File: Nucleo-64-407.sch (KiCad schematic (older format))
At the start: 70 parts, among them J1 SWD, J3 USB_B_Micro, J4 Serial 0, J5 EXP1, J6 EXP2, J7 EXP3, J8 EXP4, SW1 RESET, SW2 BOOT, U1 STM32F407VETx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

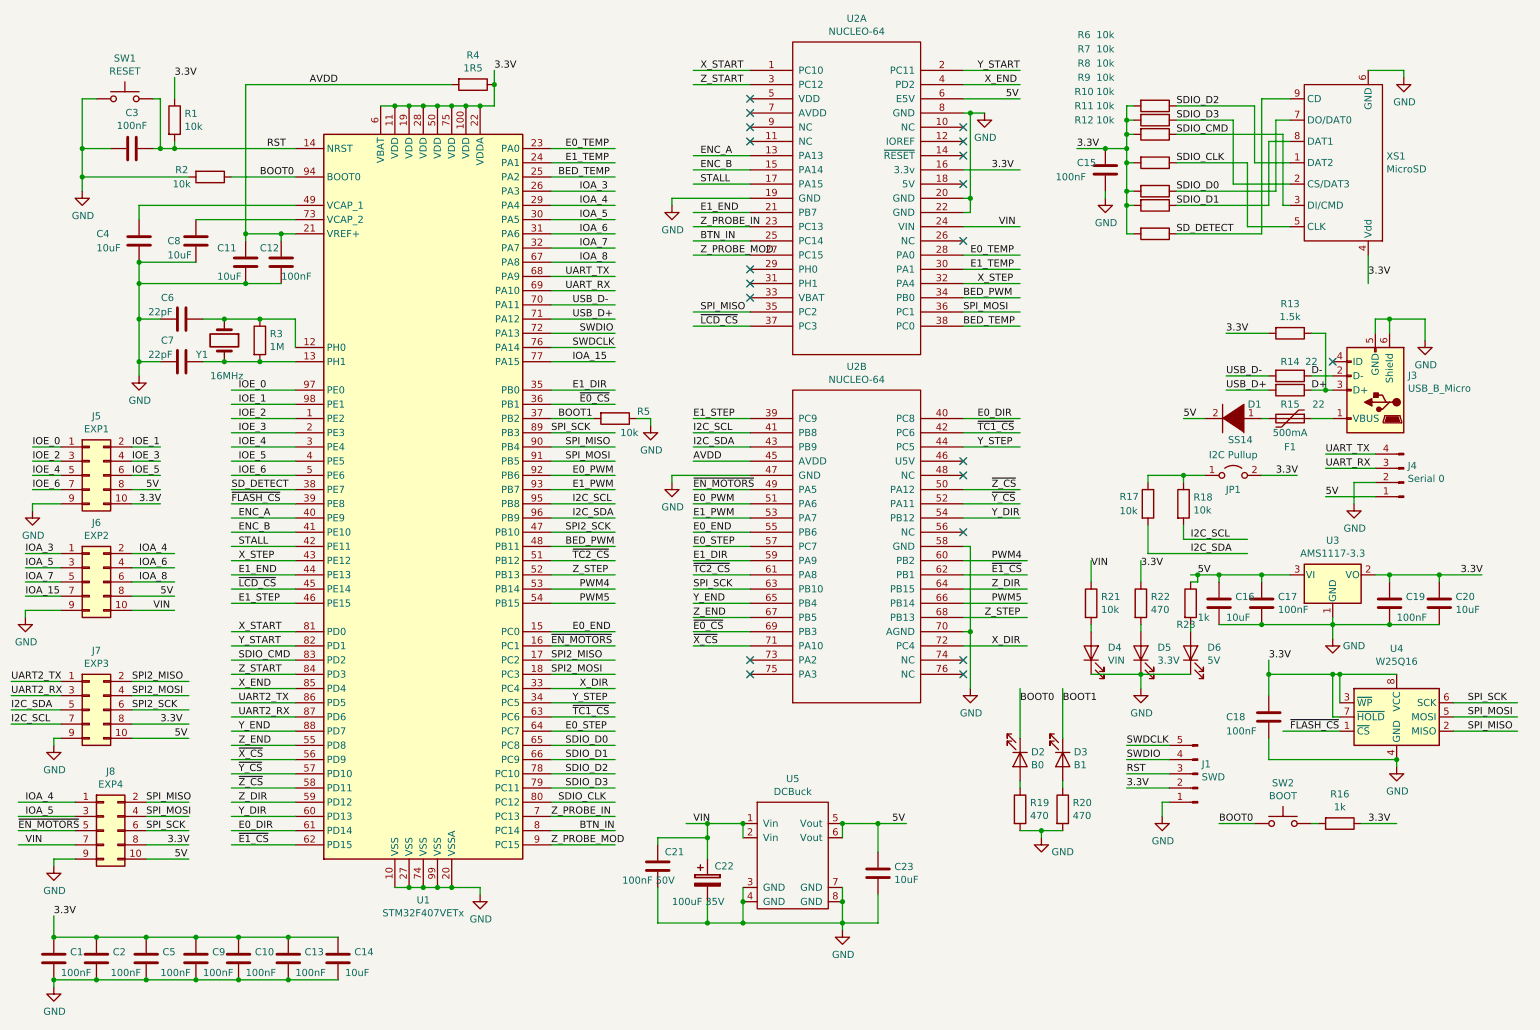
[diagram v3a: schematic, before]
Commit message: Improve the NUCLEO-64 layout a bit.
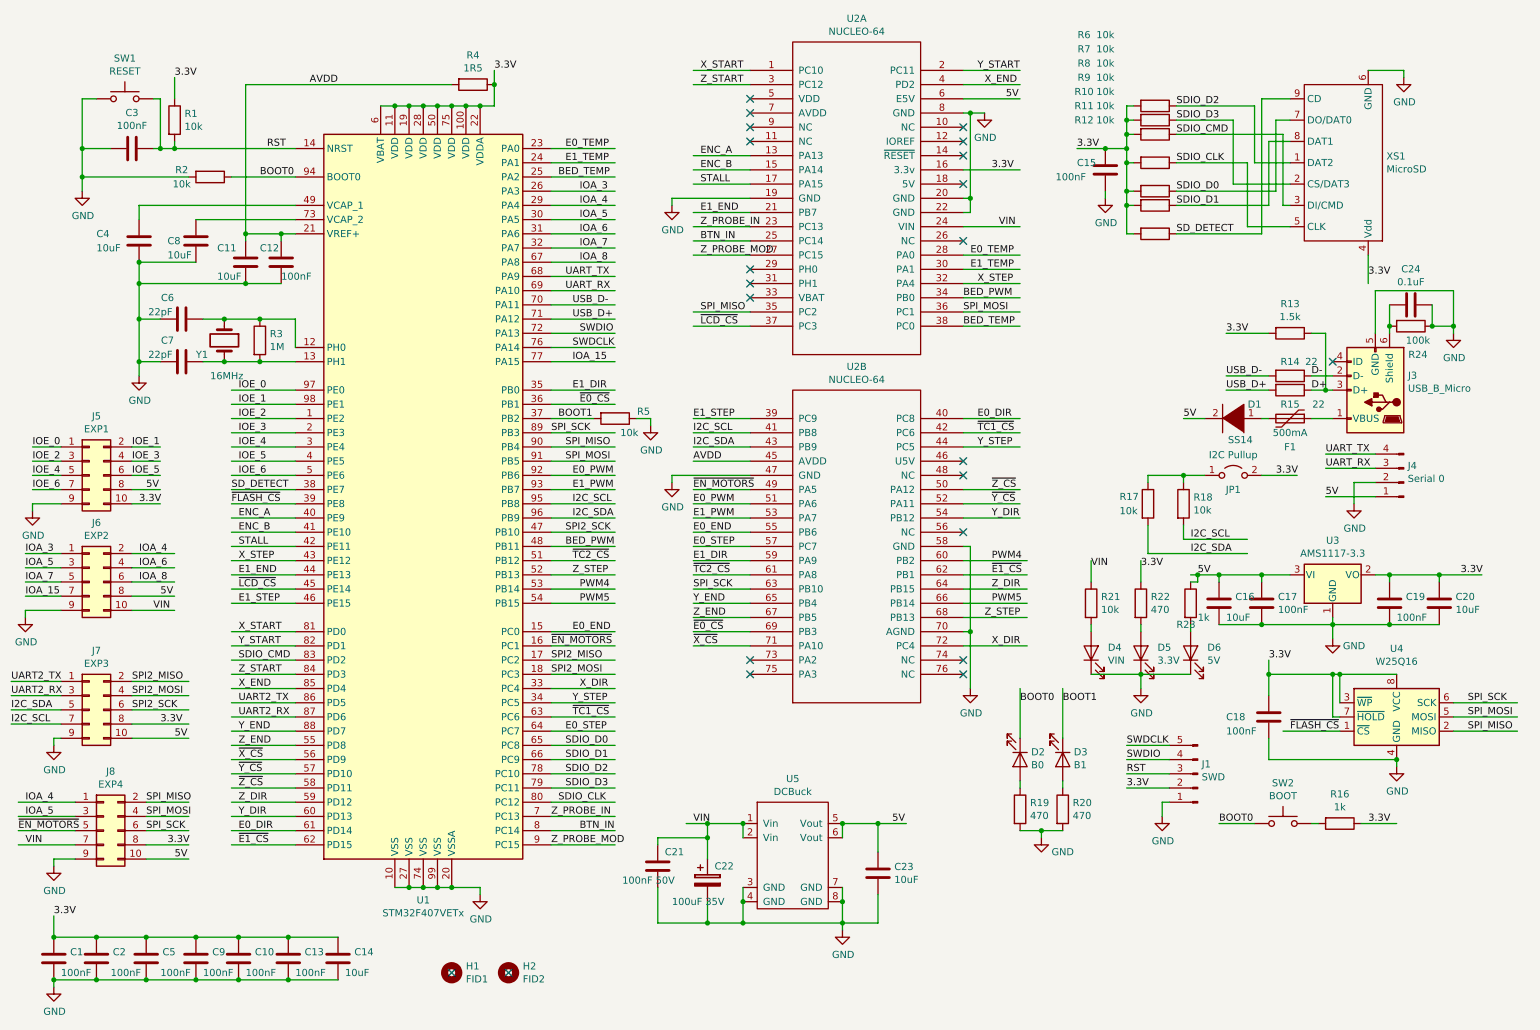
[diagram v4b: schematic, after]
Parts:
- added C24: 0.1uF, PrntrBoardV1:C_0603_1608Metric, symbol Device:C
- added H1: FID1, PrntrBoardV1:Fiducial_1mm_Dia_2.54mm_Outer_CopperTop, symbol Mechanical:MountingHole
- added H2: FID2, PrntrBoardV1:Fiducial_1mm_Dia_2.54mm_Outer_CopperTop, symbol Mechanical:MountingHole
- added R24: 100k, PrntrBoardV1:R_0603_1608Metric, symbol Device:R
- C21: footprint PrntrBoardV1:C_0603_1608Metric -> PrntrBoardV1:C_0402_1005Metric
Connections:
- wire segments 411 -> 414
- no-connect marks 20 -> 22
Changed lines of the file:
@@
 L power:GND #PWR0108
 U 1 1 5BFDEF99
-P 10450 2850
-F 0 "#PWR0108" H 10450 2600 50  0001 C CNN
-F 1 "GND" H 10455 2677 50  0000 C CNN
-F 2 "" H 10450 2850 50  0001 C CNN
-F 3 "" H 10450 2850 50  0001 C CNN
-	1    10450 2850
-	1    0    0    -1
-$EndComp
-Wire Wire Line
-	10100 2800 10100 2700
-Wire Wire Line
-	10100 2700 10200 2700
-Wire Wire Line
-	10450 2850 10450 2700
-Wire Wire Line
-	10200 2800 10200 2700
-Connection ~ 10200 2700
-Wire Wire Line
-	10200 2700 10450 2700
+P 10650 2800
+F 0 "#PWR0108" H 10650 2550 50  0001 C CNN
+F 1 "GND" H 10655 2627 50  0000 C CNN
+F 2 "" H 10650 2800 50  0001 C CNN
+F 3 "" H 10650 2800 50  0001 C CNN
+	1    10650 2800
+	1    0    0    -1
+$EndComp
 NoConn ~ 9800 3000
 $Comp
@@
 F 0 "C21" H 5100 6650 50  0000 L CNN
 F 1 "100nF 50V" H 4800 6450 50  0000 L CNN
-F 2 "PrntrBoardV1:C_0603_1608Metric" H 5088 6400 50  0001 C CNN
+F 2 "PrntrBoardV1:C_0402_1005Metric" H 5088 6400 50  0001 C CNN
 F 3 "~" H 5050 6550 50  0001 C CNN
 	1    5050 6550
@@
 Wire Wire Line
 	9200 2050 9500 2050
+$Comp
+L Device:R R24
+U 1 1 5C19E852
+P 10350 2750
+F 0 "R24" V 10550 2800 50  0000 C CNN
+F 1 "100k" V 10450 2800 50  0000 C CNN
+F 2 "PrntrBoardV1:R_0603_1608Metric" V 10280 2750 50  0001 C CNN
+F 3 "~" H 10350 2750 50  0001 C CNN
+	1    10350 2750
+	0    1    1    0
+$EndComp
+$Comp
+L Device:C C24
+U 1 1 5C19F285
+P 10350 2600
+F 0 "C24" V 10098 2600 50  0000 C CNN
+F 1 "0.1uF" V 10189 2600 50  0000 C CNN
+F 2 "PrntrBoardV1:C_0603_1608Metric" H 10388 2450 50  0001 C CNN
+F 3 "~" H 10350 2600 50  0001 C CNN
+	1    10350 2600
+	0    1    1    0
+$EndComp
+Wire Wire Line
+	10200 2800 10200 2750
+Connection ~ 10200 2750
+Wire Wire Line
+	10200 2750 10200 2600
+Wire Wire Line
+	10500 2600 10500 2750
+Wire Wire Line
+	10500 2750 10650 2750
+Wire Wire Line
+	10650 2750 10650 2800
+Connection ~ 10500 2750
+Wire Wire Line
+	10100 2800 10100 2500
+Wire Wire Line
+	10100 2500 10650 2500
+Wire Wire Line
+	10650 2500 10650 2750
+Connection ~ 10650 2750
+$Comp
+L Mechanical:MountingHole H1
+U 1 1 5C312EA4
+P 3600 7300
+F 0 "H1" H 3700 7346 50  0000 L CNN
+F 1 "FID1" H 3700 7255 50  0000 L CNN
+F 2 "PrntrBoardV1:Fiducial_1mm_Dia_2.54mm_Outer_CopperTop" H 3600 7300 50  0001 C CNN
+F 3 "~" H 3600 7300 50  0001 C CNN
+	1    3600 7300
+	1    0    0    -1
+$EndComp
+$Comp
+L Mechanical:MountingHole H2
+U 1 1 5C313AAF
+P 4000 7300
+F 0 "H2" H 4100 7346 50  0000 L CNN
+F 1 "FID2" H 4100 7255 50  0000 L CNN
+F 2 "PrntrBoardV1:Fiducial_1mm_Dia_2.54mm_Outer_CopperTop" H 4000 7300 50  0001 C CNN
+F 3 "~" H 4000 7300 50  0001 C CNN
+	1    4000 7300
+	1    0    0    -1
+$EndComp
+NoConn ~ 4000 7300
+NoConn ~ 3600 7300
 $EndSCHEMATC

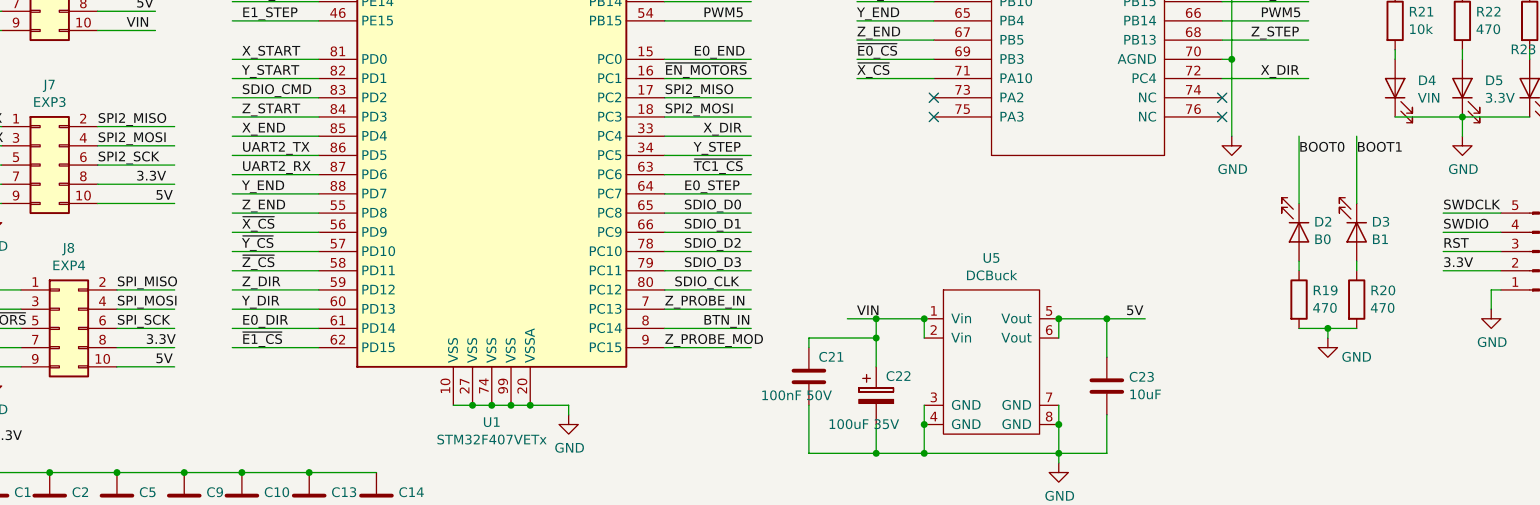
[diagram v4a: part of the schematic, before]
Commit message: Added 3.3V LDO, updated TC connectors to 6 pins. Re-arranged the layout.
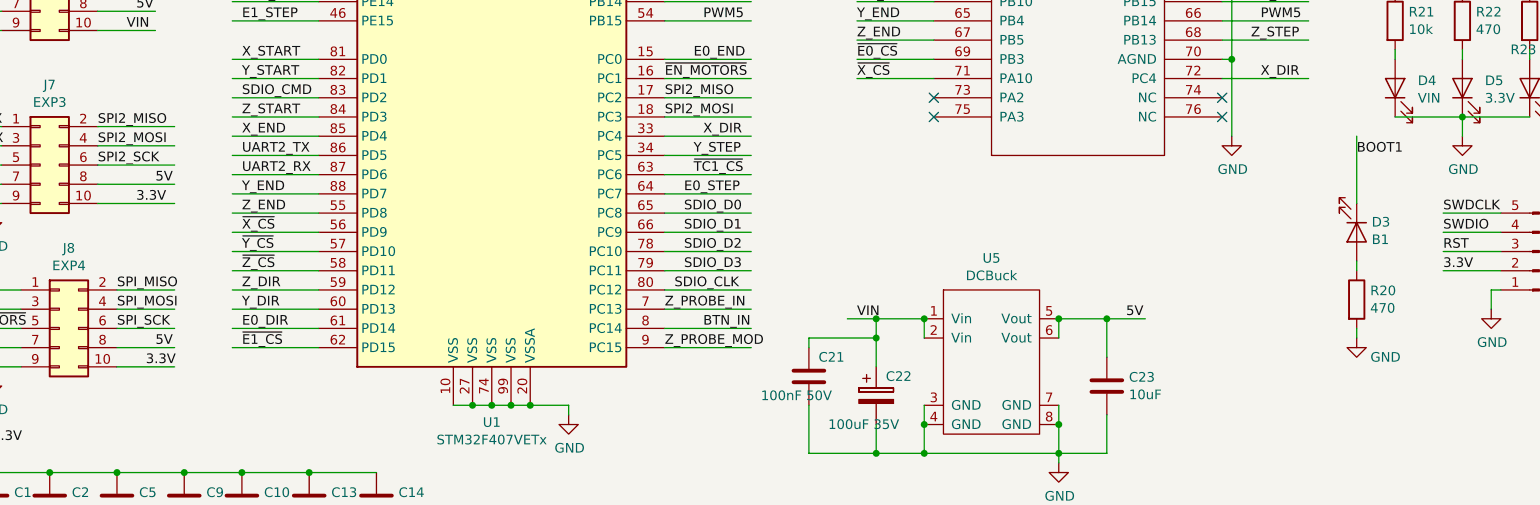
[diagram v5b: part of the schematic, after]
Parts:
- removed D2: B0, PrntrBoardV1:D_0603_1608Metric, symbol Device:LED
- removed R19: 470, PrntrBoardV1:R_0603_1608Metric, symbol Device:R
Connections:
- wire segments 414 -> 410
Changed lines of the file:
@@
 Wire Wire Line
 	1350 5550 1750 5550
-Text Label 1550 5550 0    50   ~ 0
+Text Label 1650 5550 0    50   ~ 0
+5V
+Text Label 1550 5650 0    50   ~ 0
 3.3V
-Text Label 1650 5650 0    50   ~ 0
-5V
 $Comp
 L Connector_Generic:Conn_02x05_Odd_Even J8
@@
 Wire Wire Line
 	1750 6500 1450 6500
-Text Label 1600 6400 0    50   ~ 0
+Text Label 1650 6400 0    50   ~ 0
+5V
+Text Label 1600 6500 0    50   ~ 0
 3.3V
-Text Label 1650 6500 0    50   ~ 0
-5V
 Wire Wire Line
 	950  6400 550  6400
@@
 VIN
 $Comp
-L Device:LED D2
-U 1 1 5C1EE5C9
-P 7600 5800
-F 0 "D2" V 7547 5878 50  0000 L CNN
-F 1 "B0" V 7638 5878 50  0000 L CNN
-F 2 "PrntrBoardV1:D_0603_1608Metric" H 7600 5800 50  0001 C CNN
-F 3 "~" H 7600 5800 50  0001 C CNN
-	1    7600 5800
-	0    1    1    0
-$EndComp
-$Comp
 L Device:LED D3
 U 1 1 5C1EEE8F
@@
 $EndComp
 $Comp
-L power:GND #PWR06
-U 1 1 5C1EF408
-P 7750 6350
-F 0 "#PWR06" H 7750 6100 50  0001 C CNN
-F 1 "GND" H 7900 6250 50  0000 C CNN
-F 2 "" H 7750 6350 50  0001 C CNN
-F 3 "" H 7750 6350 50  0001 C CNN
-	1    7750 6350
-	1    0    0    -1
-$EndComp
-$Comp
-L Device:R R19
-U 1 1 5C1F0045
-P 7600 6150
-F 0 "R19" H 7670 6196 50  0000 L CNN
-F 1 "470" H 7670 6105 50  0000 L CNN
-F 2 "PrntrBoardV1:R_0603_1608Metric" V 7530 6150 50  0001 C CNN
-F 3 "~" H 7600 6150 50  0001 C CNN
-	1    7600 6150
-	1    0    0    -1
-$EndComp
-$Comp
 L Device:R R20
 U 1 1 5C1F0297
@@
 $EndComp
 Wire Wire Line
-	7600 5950 7600 6000
-Wire Wire Line
 	7900 5950 7900 6000
 Wire Wire Line
-	7600 6300 7750 6300
-Wire Wire Line
-	7750 6300 7750 6350
-Connection ~ 7750 6300
-Wire Wire Line
-	7750 6300 7900 6300
-Wire Wire Line
 	7900 5650 7900 5300
-Wire Wire Line
-	7600 5650 7600 5300
-Text Label 7600 5400 0    50   ~ 0
-BOOT0
 Text Label 7900 5400 0    50   ~ 0
 BOOT1
@@
 NoConn ~ 4000 7300
 NoConn ~ 3600 7300
+$Comp
+L power:GND #PWR06
+U 1 1 5C1EF408
+P 7900 6350
+F 0 "#PWR06" H 7900 6100 50  0001 C CNN
+F 1 "GND" H 8050 6250 50  0000 C CNN
+F 2 "" H 7900 6350 50  0001 C CNN
+F 3 "" H 7900 6350 50  0001 C CNN
+	1    7900 6350
+	1    0    0    -1
+$EndComp
+Wire Wire Line
+	7900 6300 7900 6350
 $EndSCHEMATC

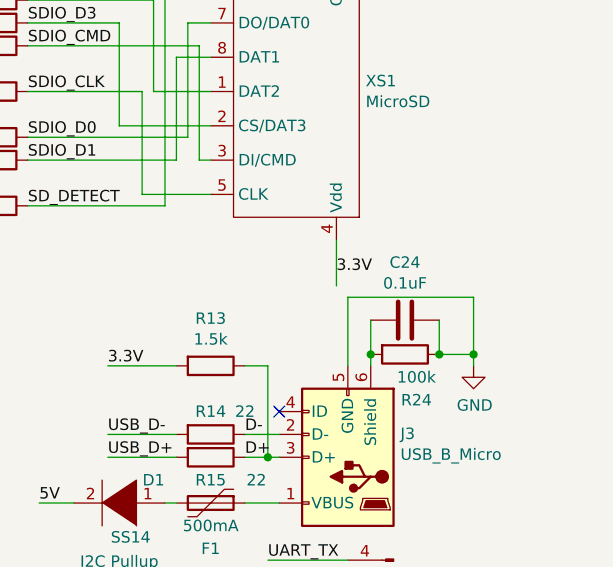
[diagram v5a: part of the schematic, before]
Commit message: Fix capavitor value.
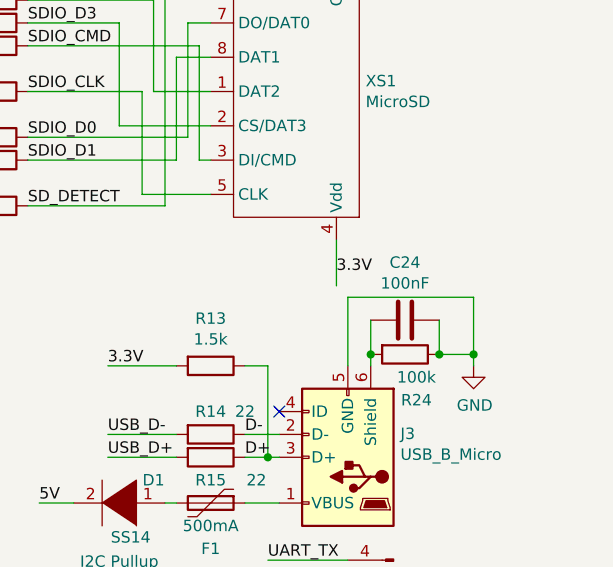
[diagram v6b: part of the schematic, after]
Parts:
- C24: value 0.1uF -> 100nF
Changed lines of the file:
@@
 P 10350 2600
 F 0 "C24" V 10098 2600 50  0000 C CNN
-F 1 "0.1uF" V 10189 2600 50  0000 C CNN
+F 1 "100nF" V 10189 2600 50  0000 C CNN
 F 2 "PrntrBoardV1:C_0603_1608Metric" H 10388 2450 50  0001 C CNN
 F 3 "~" H 10350 2600 50  0001 C CNN
